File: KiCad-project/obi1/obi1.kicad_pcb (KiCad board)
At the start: 4 copper layers, 78.7 x 86.4 mm, 138 parts, among them IC1 RAM, IC2 DAC, IC3 FLASH, J1 USB, J2 JTAG-H, J3 Conn_01x04, J4 Conn_01x04, J5 Conn_01x10, J6 Conn_01x10, J7 Conn_02x17_Counter_Clockwise, J8 Conn_02x11_Counter_Clockwise, SW1 SW_Push, SW2 SW_Push, SW3 SW_DIP_x08, U1 R3V3, U2 R1V2, U3 XC6SLX16-FTG256, U4 OSC, U5 ADC, U6 BMF055, U7 RV1, U8 RV2

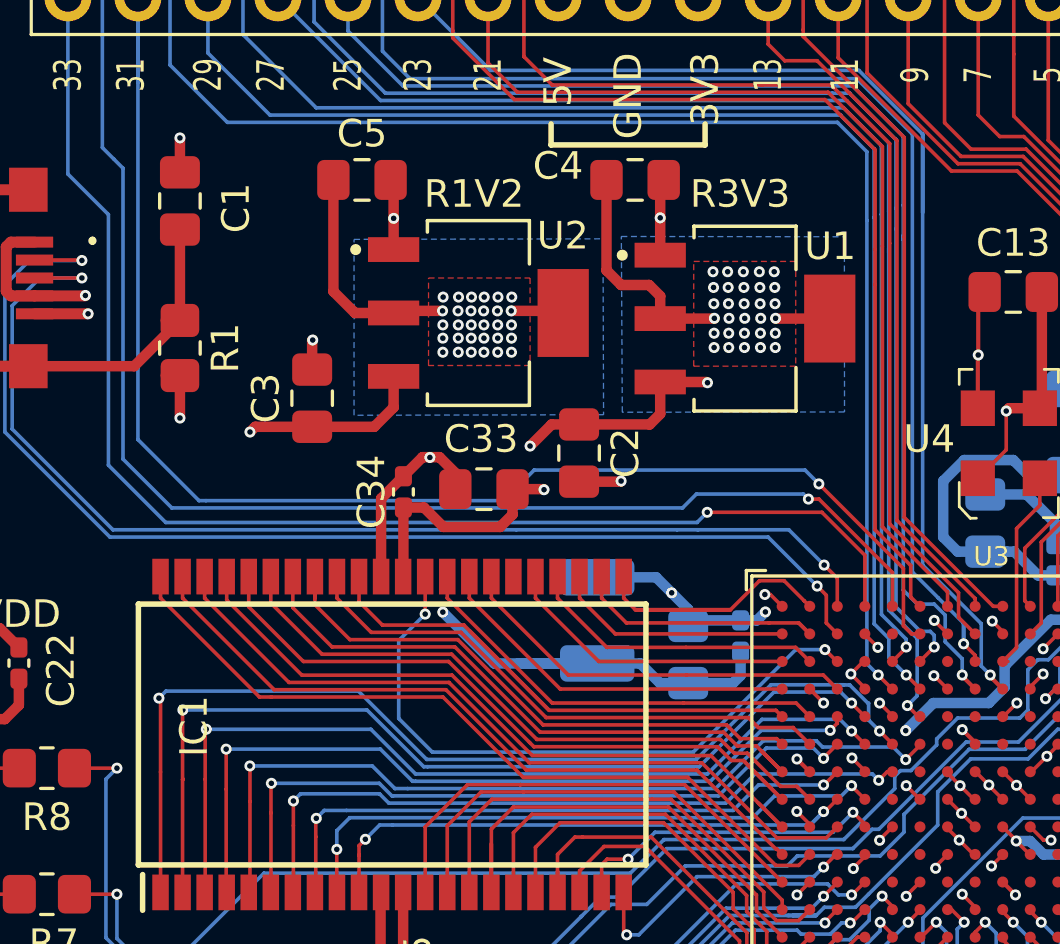
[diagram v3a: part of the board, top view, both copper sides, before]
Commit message: Changed RAM by Cypres Model -rebuild symbolic and changed footprint
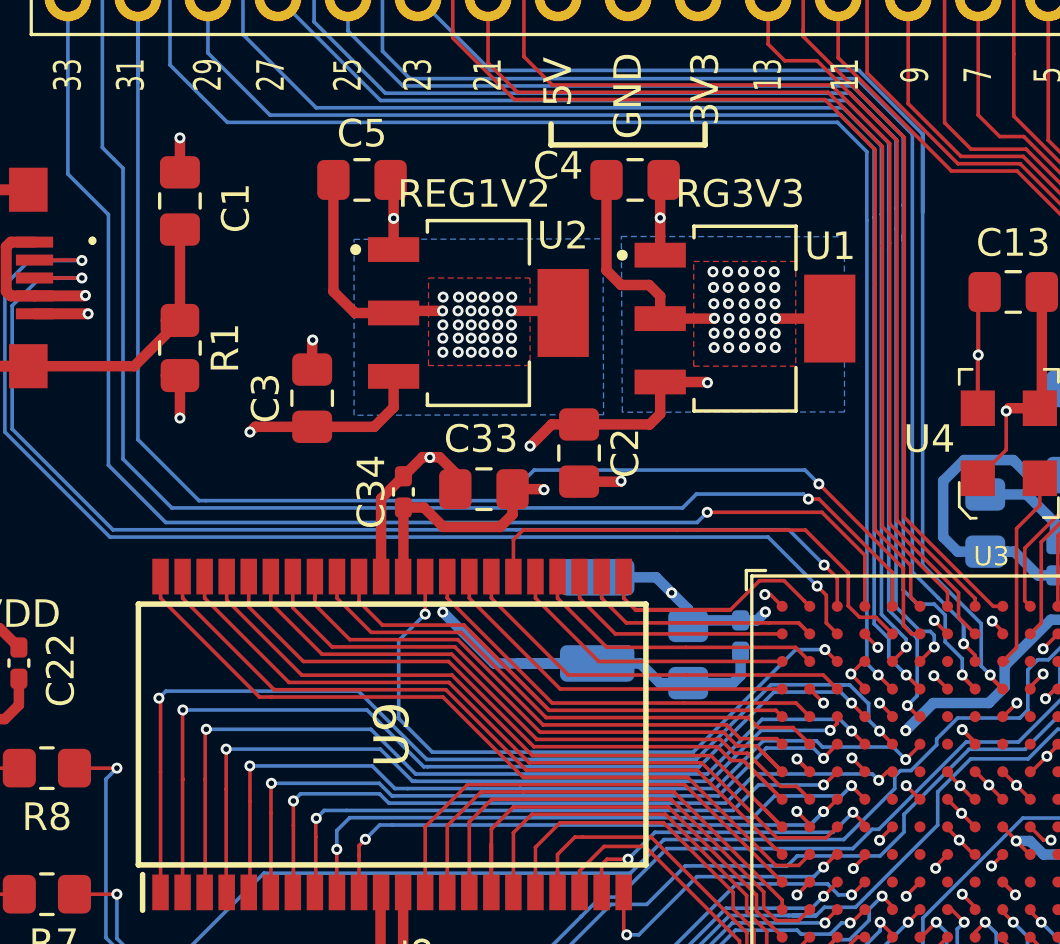
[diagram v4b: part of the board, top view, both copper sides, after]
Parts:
- removed IC1: RAM, egalan_lib:SOP80P1176X120-44N
- added U9: RAM, egalan:SOP80P1176X120-44N, F.Cu at (138.8, 92.8)
- U1: value R3V3 -> RG3V3
- U2: value R1V2 -> REG1V2
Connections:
- U3 pad A2: RAM_A10 -> RAM_A13
- U3 pad B1: RAM_A13 -> RAM_A11
- U3 pad B2: RAM_A11 -> RAM_A12
- U3 pad B5: (no net) -> RAM_A8
- U3 pad C1: RAM_A14 -> RAM_A9
- U3 pad C2: RAM_IO10 -> RAM_A10
- U3 pad D1: RAM_IO8 -> RAM_IO9
- U3 pad D3: RAM_IO9 -> RAM_IO8
- U3 pad E2: RAM_IO13 -> RAM_IO10
- U3 pad E3: RAM_A3 -> RAM_A1
- U3 pad E4: RAM_A1 -> RAM_A3
- U3 pad F2: RAM_IO3 -> RAM_IO13
- U3 pad F5: RAM_A0 -> RAM_A4
- U3 pad F6: RAM_A4 -> RAM_A0
- U3 pad H1: RAM_UB -> RAM_BHE
- U3 pad H2: RAM_LB -> RAM_BLE
- U3 pad H3: RAM_A12 -> RAM_IO3
- U3 pad J3: RAM_A15 -> RAM_A7
- U3 pad J4: RAM_A8 -> RAM_A15
- U3 pad K1: RAM_A16 -> RAM_A6
- U3 pad K2: RAM_A17 -> RAM_A5
- U3 pad K3: RAM_A9 -> RAM_A14
- U3 pad P2: RAM_A5 -> RAM_A18
- U3 pad R1: RAM_A6 -> RAM_A17
- U3 pad R2: RAM_A7 -> RAM_A16
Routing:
- net RAM_UB: track 25.3 -> 0.00 mm
- net RAM_BHE: track 0.00 -> 25.3 mm
- net RAM_LB: track 23.5 -> 0.00 mm
- net RAM_BLE: track 0.00 -> 23.5 mm
- net RAM_A15: track 27.5 -> 11.6 mm, vias 0 -> 2
- net RAM_A18: track 0.00 -> 15.3 mm
- net RAM_A17: track 28.5 -> 13.4 mm
- net RAM_A7: track 12.9 -> 27.5 mm
- net RAM_A16: track 26.4 -> 12.9 mm
- net RAM_A5: track 15.3 -> 28.5 mm
- net RAM_A6: track 13.4 -> 26.4 mm
- net RAM_A12: track 20.4 -> 9.43 mm, vias 2 -> 0
- net RAM_A4: track 30.5 -> 37.2 mm
- net RAM_A0: track 37.2 -> 30.5 mm
- net RAM_A8: track 11.6 -> 17.5 mm, vias 2 -> 0
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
